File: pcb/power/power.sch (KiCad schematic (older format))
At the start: 0 parts

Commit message: Finished LED Driver with Feedback and OLED Driver.
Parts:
- added C10, C11, C12: 10n, symbol C
- added P1: CONN_01X04, symbol CONN_01X04
- added P?: USB_B, symbol USB_B
- added R10, R7, R8: 120k, symbol R
- added R19: 39k, symbol R
- added R20, R5, R6: 3.9k, symbol R
- added R21, R22, R23: 47k, symbol R
- added R9: 240k, symbol R
- added U1: LM324QT, symbol LM324QT
- added U?: LM3578, symbol LM3578
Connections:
- net labels added: GND, PWM_OLED, V20
- wire segments 0 -> 53

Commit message: Finished driver for 2.8 V.
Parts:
- removed U?: LM3578, symbol LM3578
- gave numbers to parts that had none: 1
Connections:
- wire segments 53 -> 52
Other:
- note added: "A=(R1+R2)/R1 =31.769\nVin,max=30 mV\nVout,max=953.077 mV"
- note added: "A=(R1+R2)/R1 =7.154\nVin,max=2.8 V\nVout,max=20.031 V"
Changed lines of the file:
@@
 LIBS:valves
 LIBS:coolLib
+LIBS:power-cache
 EELAYER 25 0
 EELAYER END
 $Descr A4 11693 8268
 encoding utf-8
-Sheet 1 2
+Sheet 1 3
 Title "Power Board For SwakeUp"
 Date "2016-11-26"
@@
 F12 "LED_R_N" O R 4600 2900 60
 F13 "OPAMP_R" O R 4600 3000 60
+F14 "V20" I L 3556 2650 60
 $EndSheet
 $Comp
@@
 U 1 1 5838BEE1
 P 6800 3200
-F 0 "U1" H 7300 2450 60  0000 C CNN
-F 1 "LM324QT" H 6450 2450 60  0000 C CNN
+F 0 "U1" H 7250 2450 60  0000 C CNN
+F 1 "LM324QT" H 6500 2450 60  0000 C CNN
 F 2 "" H 6800 3200 60  0000 C CNN
 F 3 "http://www.st.com/content/ccc/resource/technical/document/datasheet/58/13/52/7e/39/8c/4c/ba/CD00000457.pdf/files/CD00000457.pdf/jcr:content/translations/en.CD00000457.pdf" H 6800 3200 60  0001 C CNN
@@
 $EndComp
 $Comp
-L GND #PWR4
+L GND #PWR5
 U 1 1 58391691
 P 8300 3700
-F 0 "#PWR4" H 8300 3450 50  0001 C CNN
+F 0 "#PWR5" H 8300 3450 50  0001 C CNN
 F 1 "GND" H 8300 3550 50  0000 C CNN
 F 2 "" H 8300 3700 50  0000 C CNN
@@
 	6100 3000 4600 3000
 Wire Wire Line
-	7500 3600 7600 3600
-Wire Wire Line
 	7900 3600 8000 3600
-Wire Wire Line
-	7500 3800 7950 3800
 Wire Wire Line
 	7950 3800 7950 3600
@@
 	5050 3650 4600 3650
 Wire Wire Line
-	4600 3300 5050 3300
+	5050 3300 4600 3300
 Connection ~ 5050 3300
 Wire Wire Line
@@
 	5150 2400 8400 2400
 Wire Wire Line
-	7500 3400 8400 3400
-Wire Wire Line
-	8400 3400 8400 2400
+	8400 2400 8400 3400
 $Comp
 L R R9
@@
 $EndComp
 Wire Wire Line
-	7500 2800 7600 2800
-Wire Wire Line
 	7900 2800 8000 2800
 $Comp
-L GND #PWR3
+L GND #PWR4
 U 1 1 58394C0A
 P 8300 2900
-F 0 "#PWR3" H 8300 2650 50  0001 C CNN
+F 0 "#PWR4" H 8300 2650 50  0001 C CNN
 F 1 "GND" H 8300 2750 50  0000 C CNN
 F 2 "" H 8300 2900 50  0000 C CNN
@@
 	7950 3100 7950 3000
 Wire Wire Line
-	7950 3000 7500 3000
-Wire Wire Line
 	8800 3100 8900 3100
 Wire Wire Line
 	9200 3100 9300 3100
 $Comp
-L GND #PWR5
+L GND #PWR6
 U 1 1 58395B51
 P 9650 3600
-F 0 "#PWR5" H 9650 3350 50  0001 C CNN
+F 0 "#PWR6" H 9650 3350 50  0001 C CNN
 F 1 "GND" H 9650 3450 50  0000 C CNN
 F 2 "" H 9650 3600 50  0000 C CNN
@@
 	1    0    0    -1
 $EndComp
-Wire Wire Line
-	7500 2600 7950 2600
 Wire Wire Line
 	7950 2600 7950 2800
@@
 Connection ~ 9650 3100
 $Comp
-L USB_B P?
+L USB_B P2
 U 1 1 58399DD1
 P 6800 4950
-F 0 "P?" H 7000 4750 50  0000 C CNN
+F 0 "P2" H 7000 4750 50  0000 C CNN
 F 1 "USB_B" H 6750 5150 50  0000 C CNN
 F 2 "" V 6750 4850 50  0000 C CNN
@@
 	0    1    1    0
 $EndComp
-$Comp
-L LM3578 U?
-U 1 1 5839A804
-P 4100 4900
-F 0 "U?" H 4250 5350 50  0000 C CNN
-F 1 "LM3578" H 4350 4450 50  0000 C CNN
-F 2 "" H 4100 4900 50  0000 C CNN
-F 3 "" H 4100 4900 50  0000 C CNN
-	1    4100 4900
-	1    0    0    -1
-$EndComp
 Wire Wire Line
 	4600 2900 5050 2900
 Connection ~ 5050 2900
 Wire Wire Line
-	5050 3650 5050 2200
+	5050 2200 5050 3650
 Text GLabel 5950 3200 0    60   Input ~ 0
 V20
@@
 	5950 3200 6100 3200
 $Comp
-L GND #PWR?
+L GND #PWR3
 U 1 1 5839C2CB
 P 7700 3200
-F 0 "#PWR?" H 7700 2950 50  0001 C CNN
+F 0 "#PWR3" H 7700 2950 50  0001 C CNN
 F 1 "GND" H 7700 3050 50  0000 C CNN
 F 2 "" H 7700 3200 50  0000 C CNN
@@
 $EndComp
 Wire Wire Line
+	7500 3800 7950 3800
+Wire Wire Line
+	7500 3600 7600 3600
+Wire Wire Line
+	8400 3400 7500 3400
+Wire Wire Line
 	7500 3200 7700 3200
-$Comp
-L GND #PWR?
-U 1 1 5839CA1C
-P 3100 5200
-F 0 "#PWR?" H 3100 4950 50  0001 C CNN
-F 1 "GND" H 3100 5050 50  0000 C CNN
-F 2 "" H 3100 5200 50  0000 C CNN
-F 3 "" H 3100 5200 50  0000 C CNN
-	1    3100 5200
-	1    0    0    -1
-$EndComp
-Wire Wire Line
-	3100 5200 3250 5200
+Wire Wire Line
+	7950 3000 7500 3000
+Wire Wire Line
+	7500 2800 7600 2800
+Wire Wire Line
+	7500 2600 7950 2600
+$Sheet
+S 3500 4850 1550 200
+U 583BCCA6
+F0 "Bucket Converter for 2.8 V" 60
+F1 "V28.sch" 60
+F2 "V28" O R 5050 4950 60
+F3 "V20" I L 3500 4950 60
+$EndSheet
+Text Notes 7700 2300 0    60   ~ 0
+A=(R1+R2)/R1 =7.154\nVin,max=2.8 V\nVout,max=20.031 V
+Text Notes 7600 4200 0    60   ~ 0
+A=(R1+R2)/R1 =31.769\nVin,max=30 mV\nVout,max=953.077 mV
 $EndSCHEMATC

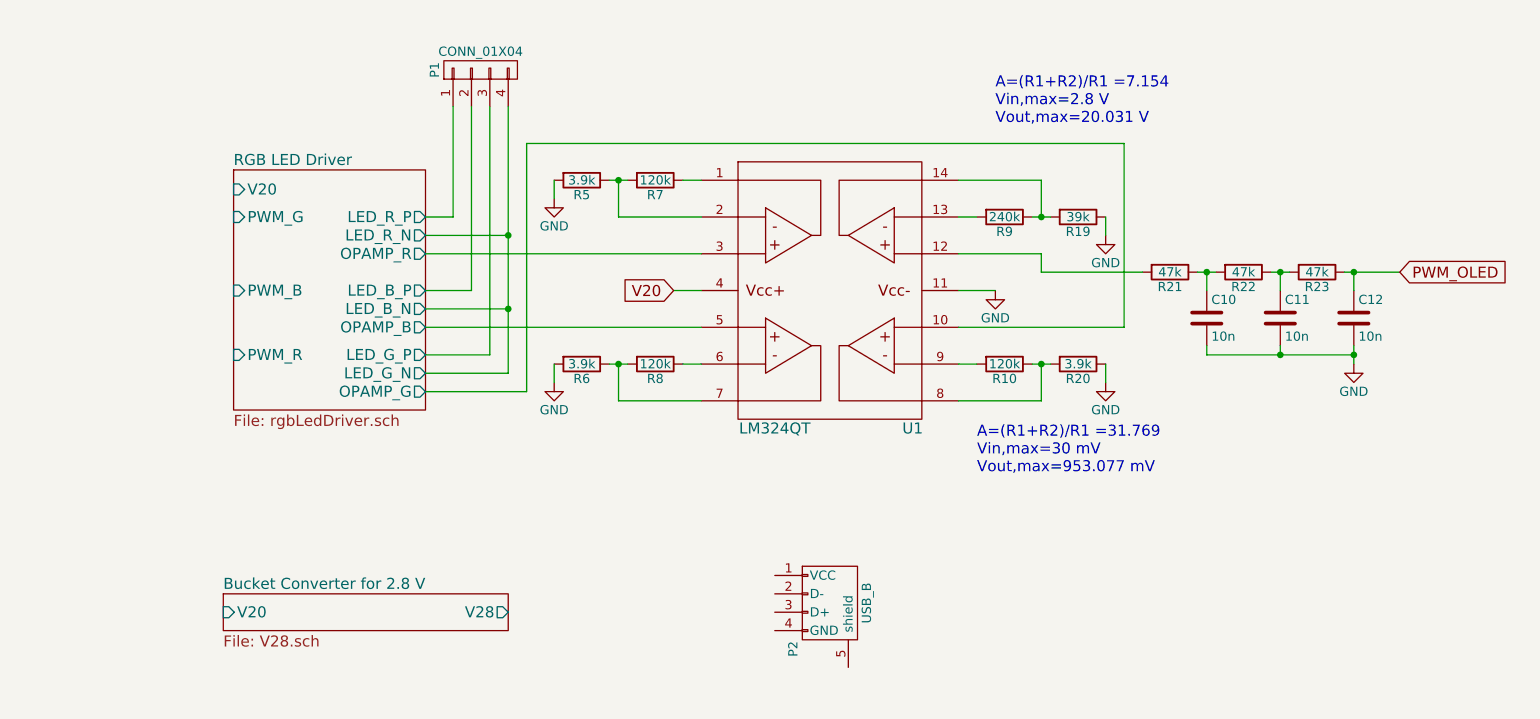
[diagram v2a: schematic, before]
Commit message: Almost finished 5V bucket converter. Found nice IC.
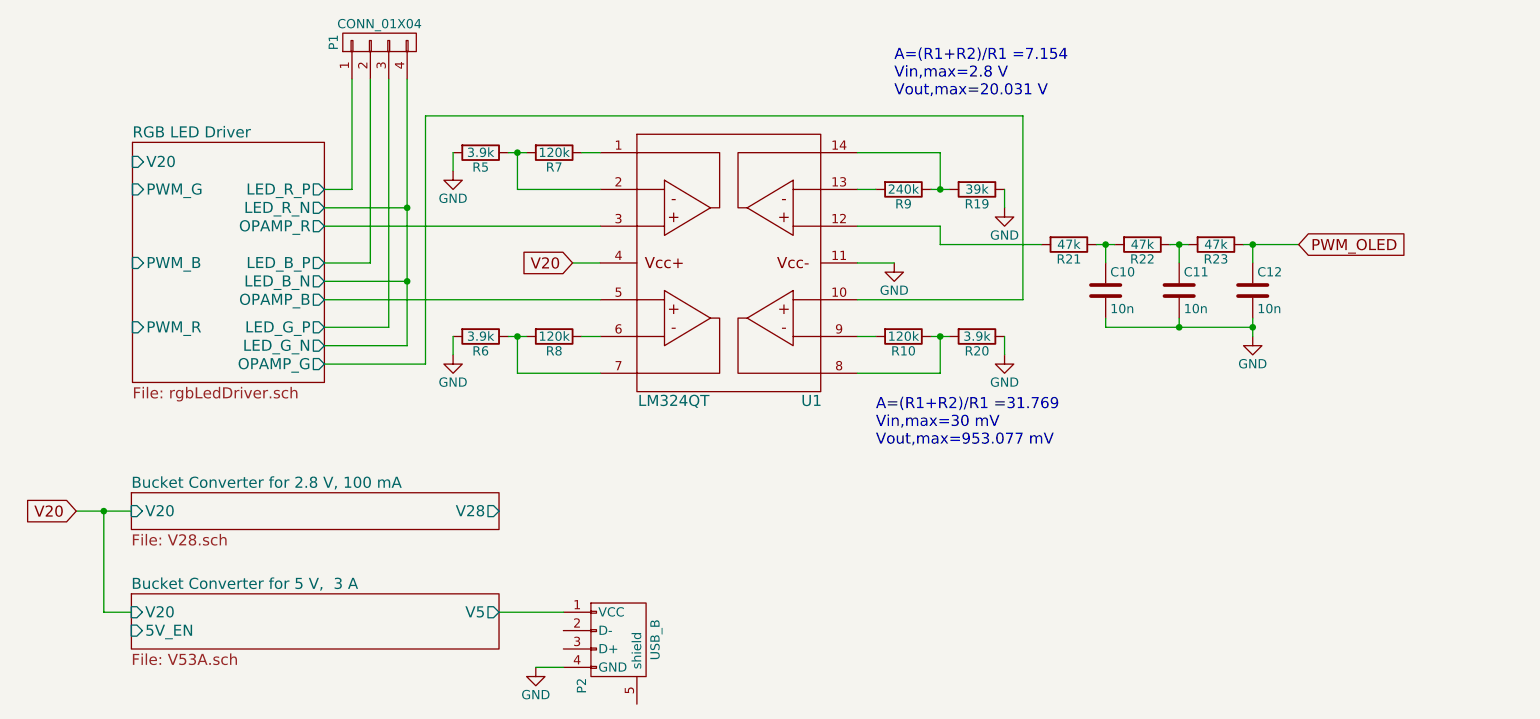
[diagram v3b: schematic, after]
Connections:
- net GND: now also P2.4 (GND)
- net Bucket Converter for 5 V,  3 A/V5: now reaches P2.1 (VCC)
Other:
- moved on the sheet: C10, C11, C12, P1, P2, R10, R19, R20, R21, R22, R23, R5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

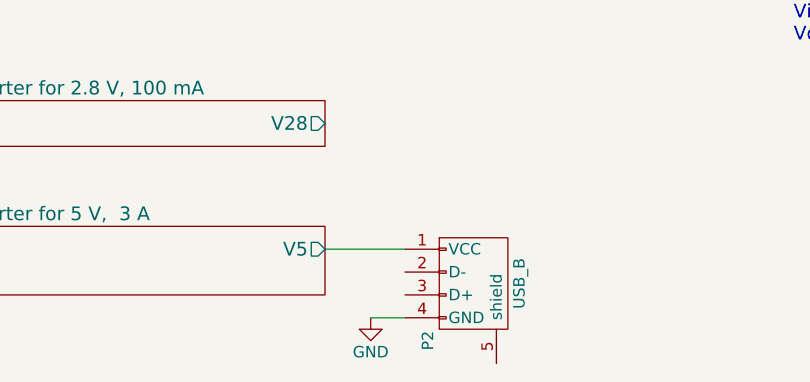
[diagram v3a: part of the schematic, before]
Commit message: Finished almost everything in the schematic. Missing: Interfacing with elmare and the correct power connector for the 20 V power supply.
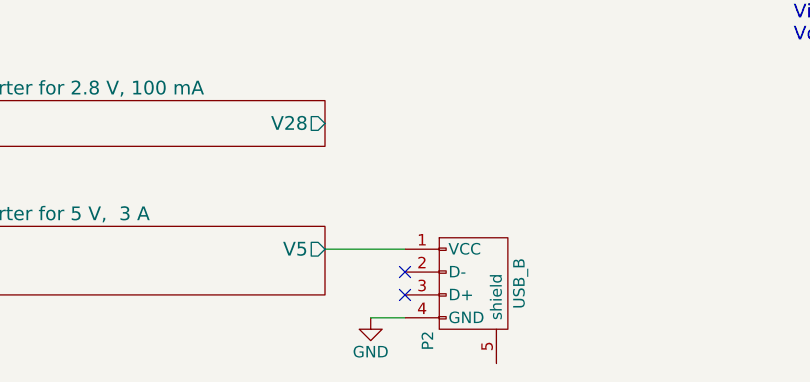
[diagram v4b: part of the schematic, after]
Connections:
- no-connect marks 0 -> 2
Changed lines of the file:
@@
 $EndComp
 $Comp
-L GND #PWR5
+L GND #PWR6
 U 1 1 58391691
 P 7750 3550
-F 0 "#PWR5" H 7750 3300 50  0001 C CNN
+F 0 "#PWR6" H 7750 3300 50  0001 C CNN
 F 1 "GND" H 7750 3400 50  0000 C CNN
 F 2 "" H 7750 3550 50  0000 C CNN
@@
 $EndComp
 $Comp
-L GND #PWR4
+L GND #PWR5
 U 1 1 58394C0A
 P 7750 2750
-F 0 "#PWR4" H 7750 2500 50  0001 C CNN
+F 0 "#PWR5" H 7750 2500 50  0001 C CNN
 F 1 "GND" H 7750 2600 50  0000 C CNN
 F 2 "" H 7750 2750 50  0000 C CNN
@@
 $EndComp
 $Comp
-L GND #PWR6
+L GND #PWR7
 U 1 1 58395B51
 P 9100 3450
-F 0 "#PWR6" H 9100 3200 50  0001 C CNN
+F 0 "#PWR7" H 9100 3200 50  0001 C CNN
 F 1 "GND" H 9100 3300 50  0000 C CNN
 F 2 "" H 9100 3450 50  0000 C CNN
@@
 V20
 $Comp
-L GND #PWR3
+L GND #PWR4
 U 1 1 5839C2CB
 P 7150 3050
-F 0 "#PWR3" H 7150 2800 50  0001 C CNN
+F 0 "#PWR4" H 7150 2800 50  0001 C CNN
 F 1 "GND" H 7150 2900 50  0000 C CNN
 F 2 "" H 7150 3050 50  0000 C CNN
@@
 	5000 4950 5350 4950
 $Comp
-L GND #PWR?
+L GND #PWR3
 U 1 1 583B960B
 P 5200 5250
-F 0 "#PWR?" H 5200 5000 50  0001 C CNN
+F 0 "#PWR3" H 5200 5000 50  0001 C CNN
 F 1 "GND" H 5200 5100 50  0000 C CNN
 F 2 "" H 5200 5250 50  0000 C CNN
@@
 Wire Wire Line
 	5200 5250 5350 5250
+NoConn ~ 5350 5050
+NoConn ~ 5350 5150
 $EndSCHEMATC

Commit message: Almost done with the schematics. Some fine tuning is left.
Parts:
- added C1, C10: 10u, symbol C
- added C2: 22n, symbol C
- added C3, C4: 22u, symbol C
- added C5: 0.1u, symbol C
- added C7: 2.2u, symbol C
- added CON1: BARREL_JACK, symbol BARREL_JACK
- added D1, D2: VS-10MQ060NPbF, symbol D_Schottky
- added L1: 4.7u, symbol INDUCTOR
- added L2: 33u, symbol INDUCTOR
- added P1, P2: CONN_01X04, symbol CONN_01X04
- added P5, P6: CONN_01X02, symbol CONN_01X02
- added R10: 150, symbol R
- added R12: 2.7k, symbol R
- added R14: 3.3k, symbol R
- added R5: 120k, symbol R
- added R8: 27k, symbol R
- added R9: 10k, symbol R
- added U1: TS30013, symbol TS30013
- added U3: LM2840, symbol LM2840
- renumbered C10 to C6, C11 to C8, C12 to C9, P1 to P3, P2 to P4, R6 to R1, R20 to R11, R19 to R13, R21 to R15, R22 to R16, R23 to R17, R5 to R2, R8 to R3, R7 to R4, R9 to R6, R10 to R7, U1 to U2
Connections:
- net GND: now also P4.5 (shield), C1.2, C10.2, C7.2, CON1.2, CON1.3, D2.2 (A), P5.2 (P2), P6.1 (P1), R10.2, R14.1, U1.14 (PWGND), U1.15 (PWGND), U1.4 (GND), U1.8 (PG), U3.2 (GND)
- net PWM_OLED: now also P1.1 (P1)
- net V20: now also C1.1, CON1.1, U1.11 (Vcc), U1.2 (Vcc), U1.3 (Vcc)
- net ADC_R: now reaches R4.1, U2.1 (O_1)
- net ADC_R: now also P2.1 (P1)
- net at U2.13 (N_4): now also R13.2, R6.1; no longer R6.2
- net at U2.6 (N_2): now also R1.1, R3.2; no longer R3.1
- net at R11.2, R7.1: now also U2.9 (N_3); no longer U2.8 (O_3)
- net ADC_G: now reaches R7.2
- net ADC_G: now also U2.8 (O_3), P2.3 (P3); no longer U2.9 (N_3)
- net Bucket Converter for 5 V,  3 A/V5: no longer names the net of P4.1 (VCC)
- net Bucket Converter for 5 V,  3 A/V5: now also C3.1, C4.1, L1.2
- new net: C10.1, L2.2, P5.1 (P1)
- new net: R12.1, R14.2
- new net: C2.2, D1.1 (K), L1.1, U1.1 (VSW), U1.12 (VSW), U1.13 (VSW), U1.16 (VSW), U1.5 (FB)
- new net: C2.1, U1.10 (BST)
- new net: U1.6 (NC), U1.7 (NC)
- new net: C3.2, C4.2, D1.2 (A)
- new net: C5.2, U3.1 (CB)
- new net: R8.1, R9.1, U3.3 (FB)
- new net: C7.1, U3.4 (~SHDN), U3.5 (Vin)
- new net: C5.1, D2.1 (K), L2.1, R8.2, U3.6 (SW)
- new net: R10.1, R9.2
- new net 5V_EN: U1.9 (EN)
- new net ADC_B: P2.2 (P2), R3.1, U2.7 (O_2)
- new net ADC_OLED: P2.4 (P4), R12.2, R5.1
- new net PWM_B: P1.3 (P3)
- new net PWM_G: P1.2 (P2)
- new net PWM_R: P1.4 (P4)
- new net VPWM: P6.2 (P2), R5.2, R6.2, U2.14 (O_4)
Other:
- note added: "A=(R1+R2)/R1 =31.769\nVin,max=30 mV\nVout,max=953.077 mV\nVref = 1.0 V"
- note added: "A=(R1+R2)/R1 =7.154\nVin,max=2.8 V\nVout,max=20.031V"
- note added: "ADC"
- note added: "PWM"
- note added: "Power for µC\n"
- note added: "SCREEN"
- note added: "Vout=0.765 V (1 + (R1 / R2))=2.8V\nR1/R2= .66"
- note removed: "A=(R1+R2)/R1 =31.769\nVin,max=30 mV\nVout,max=953.077 mV"
- note removed: "A=(R1+R2)/R1 =7.154\nVin,max=2.8 V\nVout,max=20.031 V"
- moved on the sheet: C6, C8, C9, P3, P4, R1, R11, R13, R15, R16, R17, R2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

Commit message: Finished schematics.
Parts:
- removed P5, P6: CONN_01X02, symbol CONN_01X02
- added C5: 10u, symbol C
- added D1, D3, D5: LED, symbol LED
- added P5: CONN_01X08, symbol CONN_01X08
- added P6, P7: CONN_01X03, symbol CONN_01X03
- added R1: 10k, symbol R
- added R20: 560R, symbol R
- added R6: 1.5k, symbol R
- renumbered C9 to C10, C10 to C11, C5 to C6, C6 to C7, C7 to C8, C8 to C9, D1 to D2, D2 to D4, R8 to R10, R9 to R11, R10 to R12, R11 to R13, R12 to R14, R13 to R15, R14 to R16, R15 to R17, R16 to R18, R17 to R19, R1 to R2, R2 to R3, R3 to R4, R4 to R5, R5 to R7, R6 to R8, R7 to R9
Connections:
- net 5V_EN: now also P7.2 (P2)
- net ADC_B: now also P5.2 (P2)
- net ADC_G: now also P5.3 (P3)
- net ADC_OLED: now also P5.4 (P4)
- net ADC_R: now also P5.1 (P1)
- net GND: now also C5.1, P6.2 (P2), P6.3 (P3), P7.3 (P3), R1.2, R20.2, R6.2
- net PWM_B: now also P5.6 (P6)
- net PWM_G: now also P5.7 (P7)
- net PWM_OLED: now also P5.8 (P8)
- net PWM_R: now also P5.5 (P5)
- net RGB LED Driver /OPAMP_G: no longer U2.10 (P_3)
- net V20: now also D1.2 (A)
- net at C3.1, C4.1, L1.2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: now also D3.2 (A)
- net at C11.1, L2.2: now also D5.2 (A), P7.1 (P1)
- net VPWM renamed VOLED
- net VOLED: now also C5.2, P6.1 (P1)
- new net: D3.1 (K), R6.1
- new net: D5.1 (K), R20.1
- new net: D1.1 (K), R1.1
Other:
- note added: "Bucket Converter\n---------------------------\nVout=0.765 V (1 + (27k/ 10.15k))=2.8 V\n27k/10.15= 2.66"
- note added: "Debugging Diode\n-----------------------\nDiode: 1.7 V, 2 mA\nP=2.161 mW\nCan be left out in a later version!"
- note added: "Debugging Diode\n-----------------------\nDiode: 1.7 V, 2 mA\nP=33.489 mW\nCan be left out in a later version!"
- note added: "Debugging Diode\n-----------------------\nDiode: 1.7 V, 2 mA\nP=7.26 mW\nCan be left out in a later version!"
- note added: "Non-Inv. Amp.\n-----------------------\nA=(3.9k+120k)/3.9k =31.769\nVin,max=30 mV\nVout,max=953.077 mV\nVref = 1.0 V"
- note added: "Non-Invert. Amp.\n-----------------------\nA=(240k + 39k)/39k =7.154\nVin,max=2.8 V\nVout,max=20.031V"
- note added: "Test Connector\nCan be left out in a later version."
- note added: "Voltage Divider\n-----------------------\nA=6k/120k = 20\nVin,max=20 V\nVout,max=1 V (reference of ADC)"
- note removed: "A=(R1+R2)/R1 =31.769\nVin,max=30 mV\nVout,max=953.077 mV\nVref = 1.0 V"
- note removed: "A=(R1+R2)/R1 =7.154\nVin,max=2.8 V\nVout,max=20.031V"
- note removed: "Vout=0.765 V (1 + (R1 / R2))=2.8V\nR1/R2= .66"
- moved on the sheet: C1, C10, C2, C3, C4, C7, C9, CON1, D2, L1, P1, P3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
